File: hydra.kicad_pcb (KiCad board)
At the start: 4 copper layers, 95.9 x 90.2 mm, 34 parts, among them J2 PC104 Interconnect, J3 USB-C, J8 TC2030, U1 AMS1117-3.3, U2 STM32L151RCT6, U3 USBLC6-2SC6

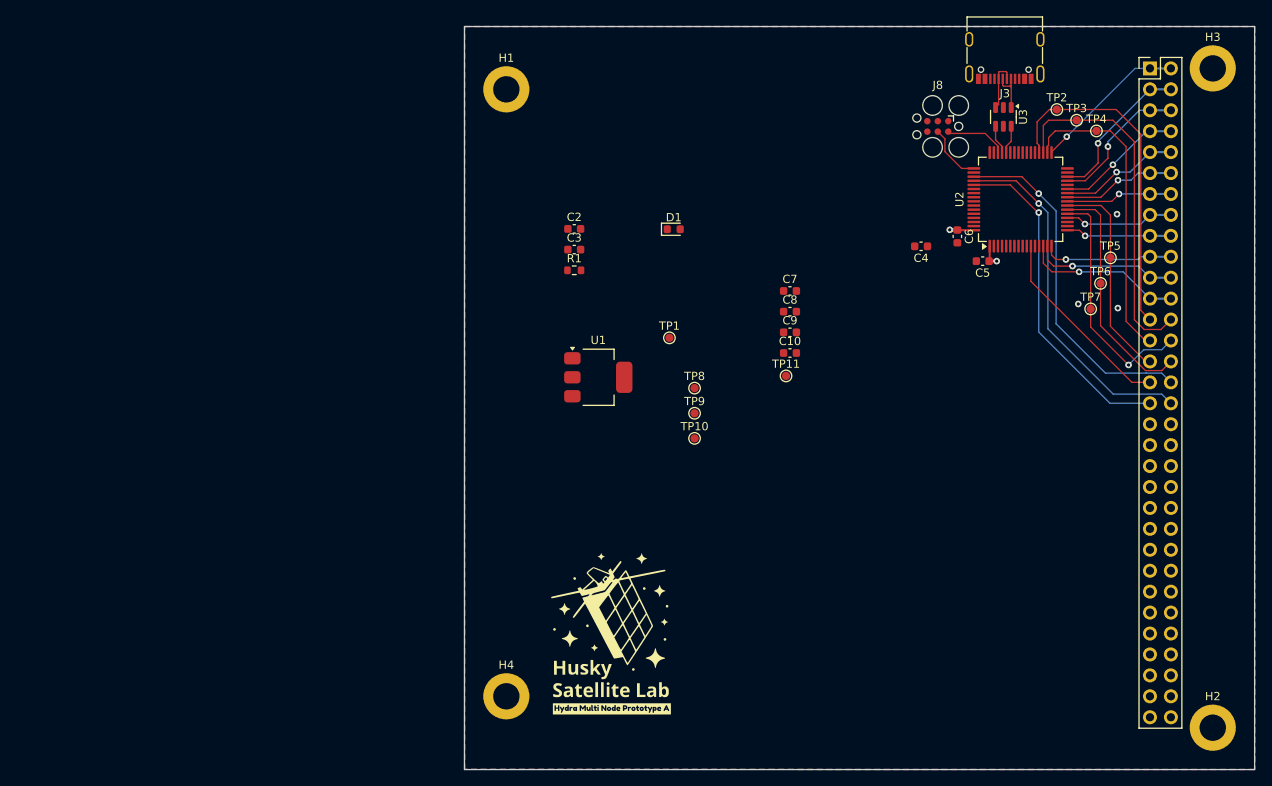
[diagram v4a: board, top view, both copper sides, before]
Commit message: feat: trying out a diff mcu
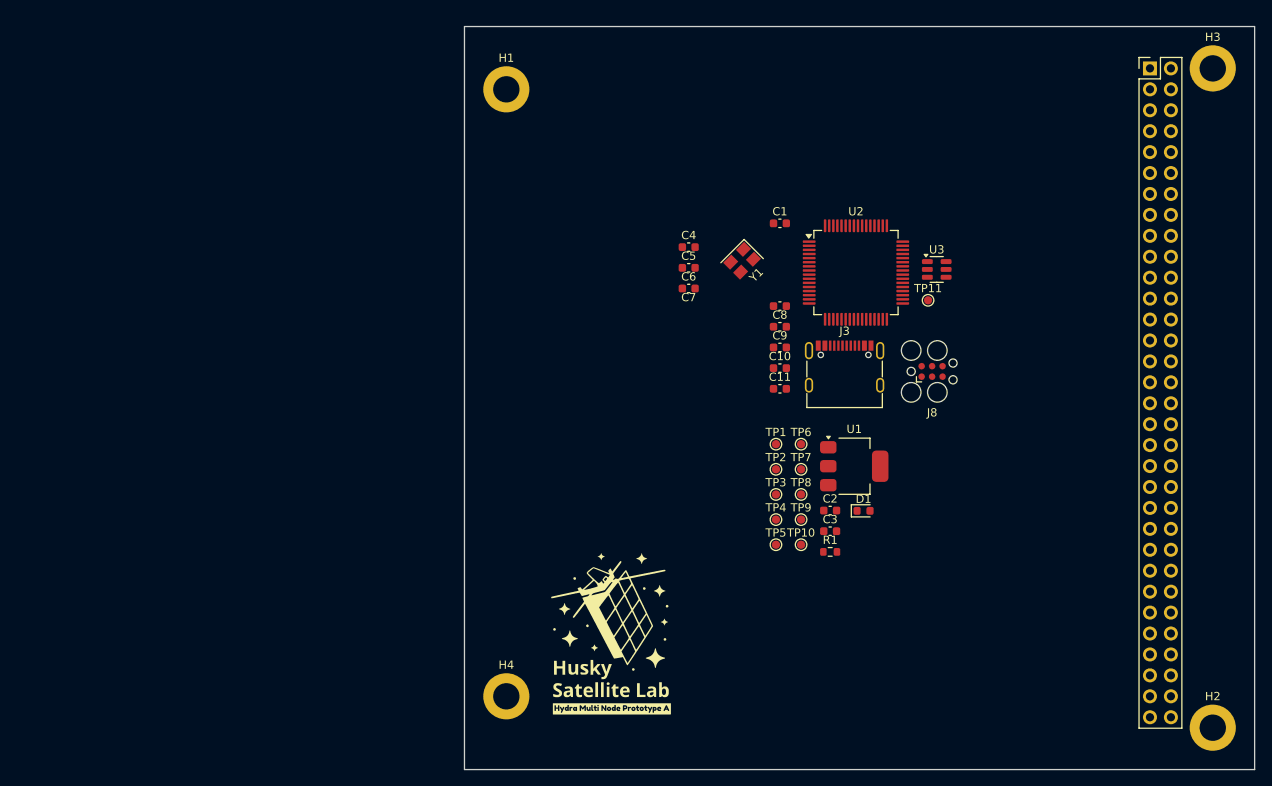
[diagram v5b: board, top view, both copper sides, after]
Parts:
- added C1: 3pF, Capacitor_SMD:C_0603_1608Metric, F.Cu at (147.4, 58.7)
- added C11: 3pF, Capacitor_SMD:C_0603_1608Metric, F.Cu at (147.4, 78.8)
- added Y1: 16MHz, Crystal:Crystal_SMD_3225-4Pin_3.2x2.5mm, F.Cu at (142.8, 63.2)
- J3: value USB-C -> TYPE-C-31-M-12
- moved TP4 61.1 mm to (146.9, 94.7)
- moved TP3 58.3 mm to (146.9, 91.6)
- moved TP2 55.4 mm to (146.9, 88.6)
- moved TP5 53.5 mm to (146.9, 97.7)
- moved C2 46.2 mm to (153.5, 93.6)
- moved C3 46.2 mm to (153.5, 96.1)
- moved R1 46.2 mm to (153.5, 98.6)
- moved J3 44.3 mm to (155.2, 77.3), turned to 0 degrees
- moved TP6 41.2 mm to (150.0, 85.5)
- moved D1 41.2 mm to (157.5, 93.6)
- moved TP7 40.2 mm to (150.0, 88.6)
- moved C5 35.7 mm to (136.3, 64.1), turned to 0 degrees
- moved C6 33.2 mm to (136.3, 66.6), turned to 0 degrees
- moved U1 32.9 mm to (156.4, 88.2)
- moved J8 29.7 mm to (165.9, 76.7), turned to 0 degrees
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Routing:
- net /R_MISO: track 43.7 -> 0.00 mm, vias 1 -> 0
- net /P_MISO: track 42.7 -> 0.00 mm
- net /R_SCLK: track 42.3 -> 0.00 mm, vias 1 -> 0
- net /P_MOSI: track 41.2 -> 0.00 mm
- net /R_MOSI: track 40.8 -> 0.00 mm, vias 1 -> 0
- net /P_SCLK: track 37.5 -> 0.00 mm
- net /S_SCLK: track 29.2 -> 0.00 mm, vias 1 -> 0
- net /S_MISO: track 29.0 -> 0.00 mm
- net /S_MOSI: track 25.8 -> 0.00 mm
- net /R_CS: track 23.8 -> 0.00 mm
- net /CS_12: track 19.3 -> 0.00 mm, vias 1 -> 0
- net /CS_1: track 18.8 -> 0.00 mm, vias 1 -> 0
- net /CS_2: track 18.5 -> 0.00 mm, vias 1 -> 0
- net /CS_11: track 17.6 -> 0.00 mm, vias 1 -> 0
- net /CS_3: track 17.3 -> 0.00 mm, vias 1 -> 0
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- removed copper zone on In2.Cu, net +3V3
- removed copper zone on B.Cu, net GND
- removed copper zone on F.Cu, net GND
- removed copper zone on In1.Cu, net GND

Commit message: Rearrange certain components
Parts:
- J3: value TYPE-C-31-M-12 -> USB-C
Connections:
- J2 pad 63: GND -> Net-(J2-Pin_63)
- J2 pad 64: GND -> Net-(J2-Pin_63)
- U2 pad 55: unconnected-(U2-PB3-Pad55) -> /Node/SD_CS
- U2 pad 61: /INTRA_SCL -> unconnected-(U2-PB8-Pad61)
- U2 pad 62: /INTRA_SDA -> unconnected-(U2-PB9-Pad62)
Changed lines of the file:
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@@
 	(net 66 "/Node/UART_TX")
 	(net 67 "unconnected-(U2-PC13-Pad2)")
-	(net 68 "/INTRA_SDA")
+	(net 68 "Net-(J2-Pin_63)")
 	(net 69 "unconnected-(U2-PC7-Pad38)")
-	(net 70 "unconnected-(U2-PB3-Pad55)")
+	(net 70 "unconnected-(U2-PB9-Pad62)")
 	(net 71 "unconnected-(U2-PA9-Pad42)")
 	(net 72 "unconnected-(U2-PC14-Pad3)")
 	(net 73 "unconnected-(U2-PB5-Pad57)")
 	(net 74 "unconnected-(U2-PC1-Pad9)")
-	(net 75 "/INTRA_SCL")
+	(net 75 "/Node/SD_CS")
 	(net 76 "/Node/UART_RX")
 	(net 77 "/Node/USB_D-")
@@
 	(net 88 "/Node/BOOT0")
 	(net 89 "unconnected-(U2-PC6-Pad37)")
+	(net 90 "unconnected-(U2-PB8-Pad61)")
 	(footprint "Capacitor_SMD:C_0603_1608Metric"
 		(layer "F.Cu")
@@
 			(layers "F.Cu" "F.Paste" "F.Mask")
 			(roundrect_rratio 0.25)
-			(net 70 "unconnected-(U2-PB3-Pad55)")
+			(net 75 "/Node/SD_CS")
 			(pinfunction "PB3")
-			(pintype "bidirectional+no_connect")
+			(pintype "bidirectional")
 		)
 		(pad "56" smd roundrect
@@
 			(layers "F.Cu" "F.Paste" "F.Mask")
 			(roundrect_rratio 0.25)
-			(net 75 "/INTRA_SCL")
+			(net 90 "unconnected-(U2-PB8-Pad61)")
 			(pinfunction "PB8")
-			(pintype "bidirectional")
+			(pintype "bidirectional+no_connect")
 		)
 		(pad "62" smd roundrect
@@
 			(layers "F.Cu" "F.Paste" "F.Mask")
 			(roundrect_rratio 0.25)
-			(net 68 "/INTRA_SDA")
+			(net 70 "unconnected-(U2-PB9-Pad62)")
 			(pinfunction "PB9")
-			(pintype "bidirectional")
+			(pintype "bidirectional+no_connect")
 		)
 		(pad "63" smd roundrect
@@
 			(layers "*.Cu" "*.Mask")
 			(remove_unused_layers no)
-			(net 2 "GND")
+			(net 68 "Net-(J2-Pin_63)")
 			(pinfunction "Pin_63")
 			(pintype "passive")
@@
 			(layers "*.Cu" "*.Mask")
 			(remove_unused_layers no)
-			(net 2 "GND")
+			(net 68 "Net-(J2-Pin_63)")
 			(pinfunction "Pin_64")
 			(pintype "passive")
@@
 			)
 		)
-		(property "Value" "TYPE-C-31-M-12"
+		(property "Value" "USB-C"
 			(at 0 5 0)
 			(layer "F.Fab")
